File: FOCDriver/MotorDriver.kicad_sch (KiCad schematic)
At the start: 51 parts, among them J2 Conn_02x06_Odd_Even, U10 DRV8316CR, U4 LM324, U5 AP7375-30SA-7

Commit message: Update
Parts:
- C92, C95: footprint Footprints:Nice_0805C -> Footprints:Nice_0603C
- R51: value 470 -> 470R
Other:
- note added: "16V"
- note added: "50V"
- note added: "6V3"
- note added: "This component is only placed for Motor channel 1!"
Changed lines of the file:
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@@
 	(generator_version "9.0")
 	(paper "A4")
+	(rectangle
+		(start 96.52 49.53)
+		(end 149.86 77.47)
+		(stroke
+			(width 0)
+			(type dash)
+		)
+		(fill
+			(type none)
+		)
+	)
+	(text "50V"
+		(exclude_from_sim no)
+		(at 227.076 68.58 0)
+		(effects
+			(font
+				(size 1.27 1.27)
+			)
+		)
+	)
 	(text "Angle Sensor: \n\nTLI5012B - 48us update time (spi)\nAS5600 - 150us update time (i2c)"
 		(exclude_from_sim no)
@@
 		)
 	)
+	(text "6V3"
+		(exclude_from_sim no)
+		(at 135.89 68.834 0)
+		(effects
+			(font
+				(size 1.27 1.27)
+			)
+		)
+	)
+	(text "16V"
+		(exclude_from_sim no)
+		(at 207.772 72.136 0)
+		(effects
+			(font
+				(size 1.27 1.27)
+			)
+		)
+	)
+	(text "50V"
+		(exclude_from_sim no)
+		(at 258.572 68.58 0)
+		(effects
+			(font
+				(size 1.27 1.27)
+			)
+		)
+	)
+	(text "50V"
+		(exclude_from_sim no)
+		(at 207.772 85.09 0)
+		(effects
+			(font
+				(size 1.27 1.27)
+			)
+		)
+	)
+	(text "50V"
+		(exclude_from_sim no)
+		(at 268.732 68.326 0)
+		(effects
+			(font
+				(size 1.27 1.27)
+			)
+		)
+	)
+	(text "6V3"
+		(exclude_from_sim no)
+		(at 161.798 130.302 0)
+		(effects
+			(font
+				(size 1.27 1.27)
+			)
+		)
+	)
+	(text "6V3"
+		(exclude_from_sim no)
+		(at 117.348 68.58 0)
+		(effects
+			(font
+				(size 1.27 1.27)
+			)
+		)
+	)
+	(text "50V"
+		(exclude_from_sim no)
+		(at 238.252 68.58 0)
+		(effects
+			(font
+				(size 1.27 1.27)
+			)
+		)
+	)
+	(text "This component is only placed for Motor channel 1!"
+		(exclude_from_sim no)
+		(at 122.936 75.438 0)
+		(effects
+			(font
+				(size 1.27 1.27)
+			)
+		)
+	)
+	(text "50V"
+		(exclude_from_sim no)
+		(at 248.412 68.58 0)
+		(effects
+			(font
+				(size 1.27 1.27)
+			)
+		)
+	)
 	(junction
 		(at 77.47 121.92)
@@
 	)
 	(no_connect
-		(at 200.66 116.84)
-	)
-	(no_connect
 		(at 200.66 135.89)
 	)
@@
 		(at 200.66 146.05)
 	)
+	(no_connect
+		(at 200.66 118.11)
+	)
 	(wire
 		(pts
@@
 	)
 	(label "MTR_AVDD"
-		(at 144.78 58.42 0)
+		(at 157.48 58.42 0)
 		(effects
 			(font
@@
 			)
 		)
-		(property "Footprint" "Footprints:Nice_0805C"
+		(property "Footprint" "Footprints:Nice_0603C"
 			(at 113.9952 68.58 0)
 			(effects
@@
 			)
 		)
-		(property "Footprint" "Footprints:Nice_0805C"
+		(property "Footprint" "Footprints:Nice_0603C"
 			(at 140.0048 68.58 0)
 			(effects
@@
 			)
 		)
-		(property "Value" "470"
+		(property "Value" "470R"
 			(at 55.88 49.53 90)
 			(effects

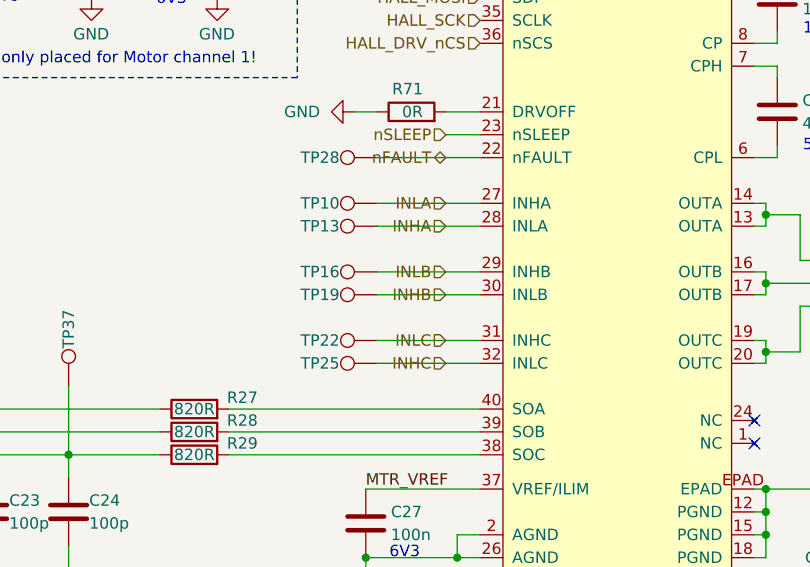
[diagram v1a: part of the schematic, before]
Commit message: Sensor PCB fixes labels
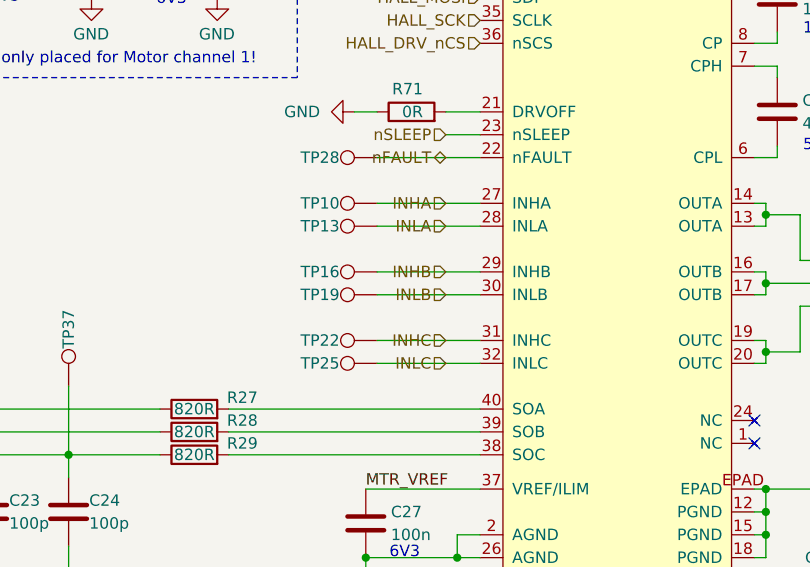
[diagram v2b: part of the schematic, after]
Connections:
- net INHA: now also TP10.1, U10.27 (INHA); no longer TP13.1, U10.28 (INLA)
- net INHB: now also TP16.1, U10.29 (INHB); no longer TP19.1, U10.30 (INLB)
- net INHC: now also TP22.1, U10.31 (INHC); no longer TP25.1, U10.32 (INLC)
- net INLA: now also TP13.1, U10.28 (INLA); no longer TP10.1, U10.27 (INHA)
- net INLB: now also TP19.1, U10.30 (INLB); no longer TP16.1, U10.29 (INHB)
- net INLC: now also TP25.1, U10.32 (INLC); no longer TP22.1, U10.31 (INHC)
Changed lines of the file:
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@@
 	(hierarchical_label "INLC"
 		(shape input)
+		(at 166.37 109.22 180)
+		(effects
+			(font
+				(size 1.27 1.27)
+			)
+			(justify right)
+		)
+	)
+	(hierarchical_label "VM"
+		(shape input)
+		(at 203.2 53.34 90)
+		(effects
+			(font
+				(size 1.27 1.27)
+			)
+			(justify left)
+		)
+	)
+	(hierarchical_label "HALL_SDA"
+		(shape input)
+		(at 96.52 40.64 0)
+		(effects
+			(font
+				(size 1.27 1.27)
+			)
+			(justify left)
+		)
+	)
+	(hierarchical_label "HALL_SCK"
+		(shape input)
+		(at 170.18 71.12 180)
+		(effects
+			(font
+				(size 1.27 1.27)
+			)
+			(justify right)
+		)
+	)
+	(hierarchical_label "SOB"
+		(shape input)
+		(at 72.39 121.92 180)
+		(effects
+			(font
+				(size 1.27 1.27)
+			)
+			(justify right)
+		)
+	)
+	(hierarchical_label "HALL_nCS"
+		(shape input)
+		(at 73.66 43.18 0)
+		(effects
+			(font
+				(size 1.27 1.27)
+			)
+			(justify left)
+		)
+	)
+	(hierarchical_label "TEMPERATURE"
+		(shape input)
+		(at 74.93 162.56 180)
+		(effects
+			(font
+				(size 1.27 1.27)
+			)
+			(justify right)
+		)
+	)
+	(hierarchical_label "V"
+		(shape input)
+		(at 209.55 100.33 0)
+		(effects
+			(font
+				(size 1.27 1.27)
+			)
+			(justify left)
+		)
+	)
+	(hierarchical_label "HALL_DRV_nCS"
+		(shape input)
+		(at 170.18 73.66 180)
+		(effects
+			(font
+				(size 1.27 1.27)
+			)
+			(justify right)
+		)
+	)
+	(hierarchical_label "HALL_SCK"
+		(shape input)
+		(at 53.34 38.1 180)
+		(effects
+			(font
+				(size 1.27 1.27)
+			)
+			(justify right)
+		)
+	)
+	(hierarchical_label "HALL_MISO"
+		(shape input)
+		(at 170.18 66.04 180)
+		(effects
+			(font
+				(size 1.27 1.27)
+			)
+			(justify right)
+		)
+	)
+	(hierarchical_label "SOA"
+		(shape input)
+		(at 72.39 107.95 180)
+		(effects
+			(font
+				(size 1.27 1.27)
+			)
+			(justify right)
+		)
+	)
+	(hierarchical_label "INLA"
+		(shape input)
+		(at 166.37 93.98 180)
+		(effects
+			(font
+				(size 1.27 1.27)
+			)
+			(justify right)
+		)
+	)
+	(hierarchical_label "nSLEEP"
+		(shape input)
+		(at 166.37 83.82 180)
+		(effects
+			(font
+				(size 1.27 1.27)
+			)
+			(justify right)
+		)
+	)
+	(hierarchical_label "HALL_MOSI"
+		(shape input)
+		(at 53.34 43.18 180)
+		(effects
+			(font
+				(size 1.27 1.27)
+			)
+			(justify right)
+		)
+	)
+	(hierarchical_label "SOC"
+		(shape input)
+		(at 72.39 135.89 180)
+		(effects
+			(font
+				(size 1.27 1.27)
+			)
+			(justify right)
+		)
+	)
+	(hierarchical_label "INHC"
+		(shape input)
 		(at 166.37 106.68 180)
-		(effects
-			(font
-				(size 1.27 1.27)
-			)
-			(justify right)
-		)
-	)
-	(hierarchical_label "VM"
-		(shape input)
-		(at 203.2 53.34 90)
-		(effects
-			(font
-				(size 1.27 1.27)
-			)
-			(justify left)
-		)
-	)
-	(hierarchical_label "HALL_SDA"
-		(shape input)
-		(at 96.52 40.64 0)
-		(effects
-			(font
-				(size 1.27 1.27)
-			)
-			(justify left)
-		)
-	)
-	(hierarchical_label "HALL_SCK"
-		(shape input)
-		(at 170.18 71.12 180)
-		(effects
-			(font
-				(size 1.27 1.27)
-			)
-			(justify right)
-		)
-	)
-	(hierarchical_label "SOB"
-		(shape input)
-		(at 72.39 121.92 180)
-		(effects
-			(font
-				(size 1.27 1.27)
-			)
-			(justify right)
-		)
-	)
-	(hierarchical_label "HALL_nCS"
-		(shape input)
-		(at 73.66 43.18 0)
-		(effects
-			(font
-				(size 1.27 1.27)
-			)
-			(justify left)
-		)
-	)
-	(hierarchical_label "TEMPERATURE"
-		(shape input)
-		(at 74.93 162.56 180)
-		(effects
-			(font
-				(size 1.27 1.27)
-			)
-			(justify right)
-		)
-	)
-	(hierarchical_label "V"
-		(shape input)
-		(at 209.55 100.33 0)
-		(effects
-			(font
-				(size 1.27 1.27)
-			)
-			(justify left)
-		)
-	)
-	(hierarchical_label "HALL_DRV_nCS"
-		(shape input)
-		(at 170.18 73.66 180)
-		(effects
-			(font
-				(size 1.27 1.27)
-			)
-			(justify right)
-		)
-	)
-	(hierarchical_label "HALL_SCK"
-		(shape input)
-		(at 53.34 38.1 180)
-		(effects
-			(font
-				(size 1.27 1.27)
-			)
-			(justify right)
-		)
-	)
-	(hierarchical_label "HALL_MISO"
-		(shape input)
-		(at 170.18 66.04 180)
-		(effects
-			(font
-				(size 1.27 1.27)
-			)
-			(justify right)
-		)
-	)
-	(hierarchical_label "SOA"
-		(shape input)
-		(at 72.39 107.95 180)
-		(effects
-			(font
-				(size 1.27 1.27)
-			)
-			(justify right)
-		)
-	)
-	(hierarchical_label "INLA"
-		(shape input)
-		(at 166.37 91.44 180)
-		(effects
-			(font
-				(size 1.27 1.27)
-			)
-			(justify right)
-		)
-	)
-	(hierarchical_label "nSLEEP"
-		(shape input)
-		(at 166.37 83.82 180)
-		(effects
-			(font
-				(size 1.27 1.27)
-			)
-			(justify right)
-		)
-	)
-	(hierarchical_label "HALL_MOSI"
-		(shape input)
-		(at 53.34 43.18 180)
-		(effects
-			(font
-				(size 1.27 1.27)
-			)
-			(justify right)
-		)
-	)
-	(hierarchical_label "SOC"
-		(shape input)
-		(at 72.39 135.89 180)
-		(effects
-			(font
-				(size 1.27 1.27)
-			)
-			(justify right)
-		)
-	)
-	(hierarchical_label "INHC"
-		(shape input)
-		(at 166.37 109.22 180)
 		(effects
 			(font
@@
 	(hierarchical_label "INHB"
 		(shape input)
+		(at 166.37 99.06 180)
+		(effects
+			(font
+				(size 1.27 1.27)
+			)
+			(justify right)
+		)
+	)
+	(hierarchical_label "HALL_SCL"
+		(shape input)
+		(at 96.52 38.1 0)
+		(effects
+			(font
+				(size 1.27 1.27)
+			)
+			(justify left)
+		)
+	)
+	(hierarchical_label "WIPER"
+		(shape input)
+		(at 29.21 30.48 180)
+		(effects
+			(font
+				(size 1.27 1.27)
+			)
+			(justify right)
+		)
+	)
+	(hierarchical_label "HALL_MISO"
+		(shape input)
+		(at 53.34 40.64 180)
+		(effects
+			(font
+				(size 1.27 1.27)
+			)
+			(justify right)
+		)
+	)
+	(hierarchical_label "INHA"
+		(shape input)
+		(at 166.37 91.44 180)
+		(effects
+			(font
+				(size 1.27 1.27)
+			)
+			(justify right)
+		)
+	)
+	(hierarchical_label "INLB"
+		(shape input)
 		(at 166.37 101.6 180)
 		(effects
 			(font
-				(size 1.27 1.27)
-			)
-			(justify right)
-		)
-	)
-	(hierarchical_label "HALL_SCL"
-		(shape input)
-		(at 96.52 38.1 0)
-		(effects
-			(font
-				(size 1.27 1.27)
-			)
-			(justify left)
-		)
-	)
-	(hierarchical_label "WIPER"
-		(shape input)
-		(at 29.21 30.48 180)
-		(effects
-			(font
-				(size 1.27 1.27)
-			)
-			(justify right)
-		)
-	)
-	(hierarchical_label "HALL_MISO"
-		(shape input)
-		(at 53.34 40.64 180)
-		(effects
-			(font
-				(size 1.27 1.27)
-			)
-			(justify right)
-		)
-	)
-	(hierarchical_label "INHA"
-		(shape input)
-		(at 166.37 93.98 180)
-		(effects
-			(font
-				(size 1.27 1.27)
-			)
-			(justify right)
-		)
-	)
-	(hierarchical_label "INLB"
-		(shape input)
-		(at 166.37 99.06 180)
-		(effects
-			(font

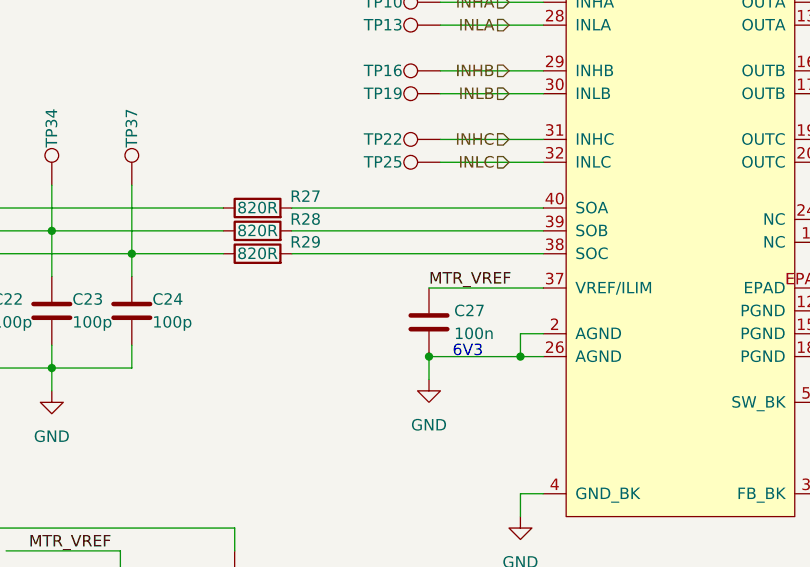
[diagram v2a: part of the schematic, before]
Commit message: Untented vias for DRVOFF signal Added unallocated IOs for DRVOFF potentially
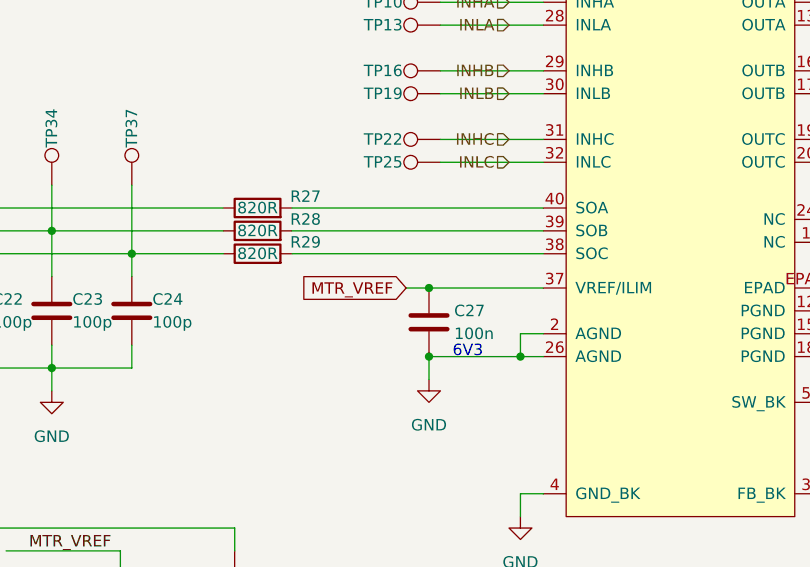
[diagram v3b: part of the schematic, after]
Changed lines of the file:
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@@
+	)
+	(junction
+		(at 157.48 123.19)
+		(diameter 0)
+		(color 0 0 0 0)
 	)
 	(junction
@@
 	(wire
 		(pts
+			(xy 154.94 123.19) (xy 157.48 123.19)
+		)
+		(stroke
+			(width 0)
+			(type default)
+		)
+	)
+	(wire
+		(pts
 			(xy 115.57 132.08) (xy 115.57 134.62)
 		)
@@
 	(label "NTC"
 		(at 110.49 160.02 0)
-		(effects
-			(font
-				(size 1.27 1.27)
-			)
-			(justify left bottom)
-		)
-	)
-	(label "MTR_VREF"
-		(at 157.48 123.19 0)
 		(effects
 			(font
@@
 			)
 		)
+	)
+	(global_label "MTR_VREF"
+		(shape input)
+		(at 154.94 123.19 180)
+		(fields_autoplaced yes)
+		(effects
+			(font
+				(size 1.27 1.27)
+			)
+			(justify right)
+		)
+		(property "Intersheetrefs" "${INTERSHEET_REFS}"
+			(at 142.702 123.19 0)
+			(effects
+				(font
+					(size 1.27 1.27)
+				)
+				(justify right)
+			)
+		)
